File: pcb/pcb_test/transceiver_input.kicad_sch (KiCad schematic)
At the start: 26 parts, among them U2 LM324

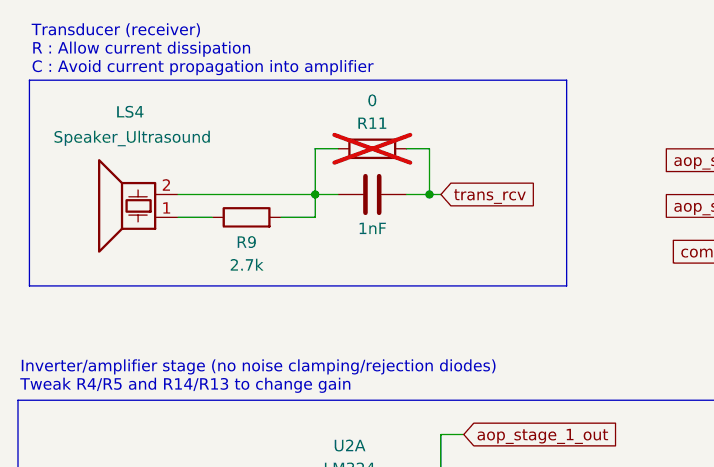
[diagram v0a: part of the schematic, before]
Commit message: fix: patch psb test issues and delete generated files
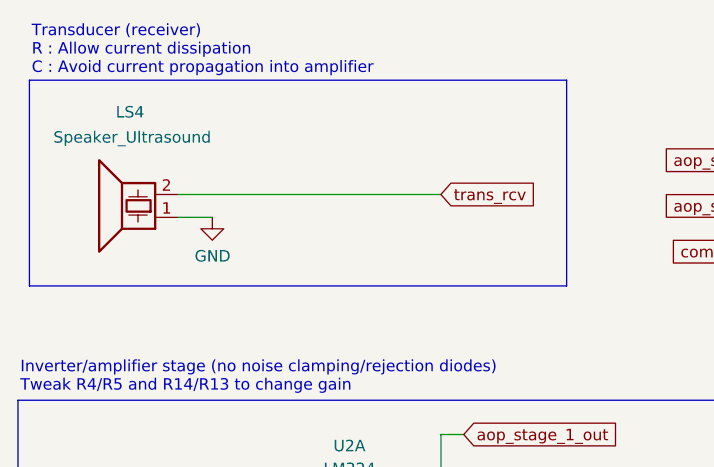
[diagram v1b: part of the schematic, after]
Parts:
- removed C10: 1nF, Capacitor_THT:C_Disc_D4.3mm_W1.9mm_P5.00mm, symbol Device:C
- removed R11: 0, Resistor_THT:R_Axial_DIN0207_L6.3mm_D2.5mm_P10.16mm_Horizontal, symbol Device:R
- removed R9: 2.7k, Resistor_THT:R_Axial_DIN0207_L6.3mm_D2.5mm_P10.16mm_Horizontal, symbol Device:R
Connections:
- net GND: now also LS4.1
- net trans_rcv: now also LS4.2
